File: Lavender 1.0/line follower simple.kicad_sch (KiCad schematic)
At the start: 33 parts, among them J1 XT30UPB-M, J2 Conn_01x20_MountingPin, J3 Conn_01x02_Pin, J4 Conn_01x02_Pin, J6 Conn_01x20_MountingPin, J7 Conn_01x20_MountingPin, J9 Conn_01x20_MountingPin, SW2 SW_Push, SW3 SW_Push, SW5 SW_Push_DPDT, SW6 SW_Push_DPDT, U1 74HC4067

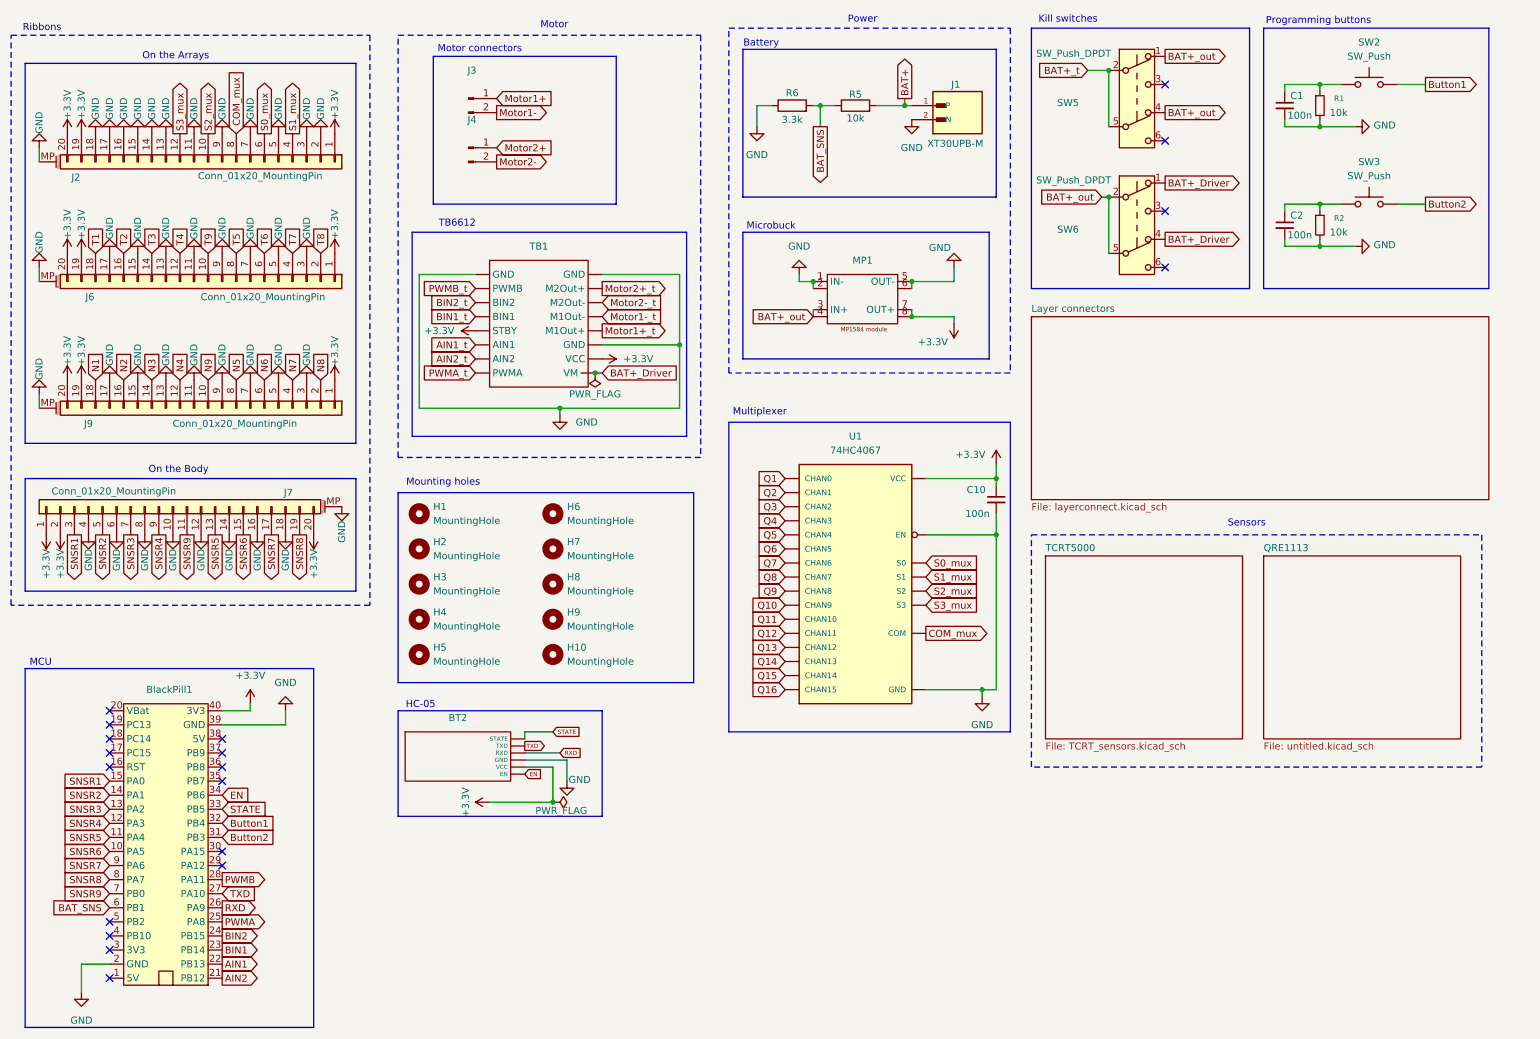
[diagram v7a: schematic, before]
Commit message: Start custom sensor array
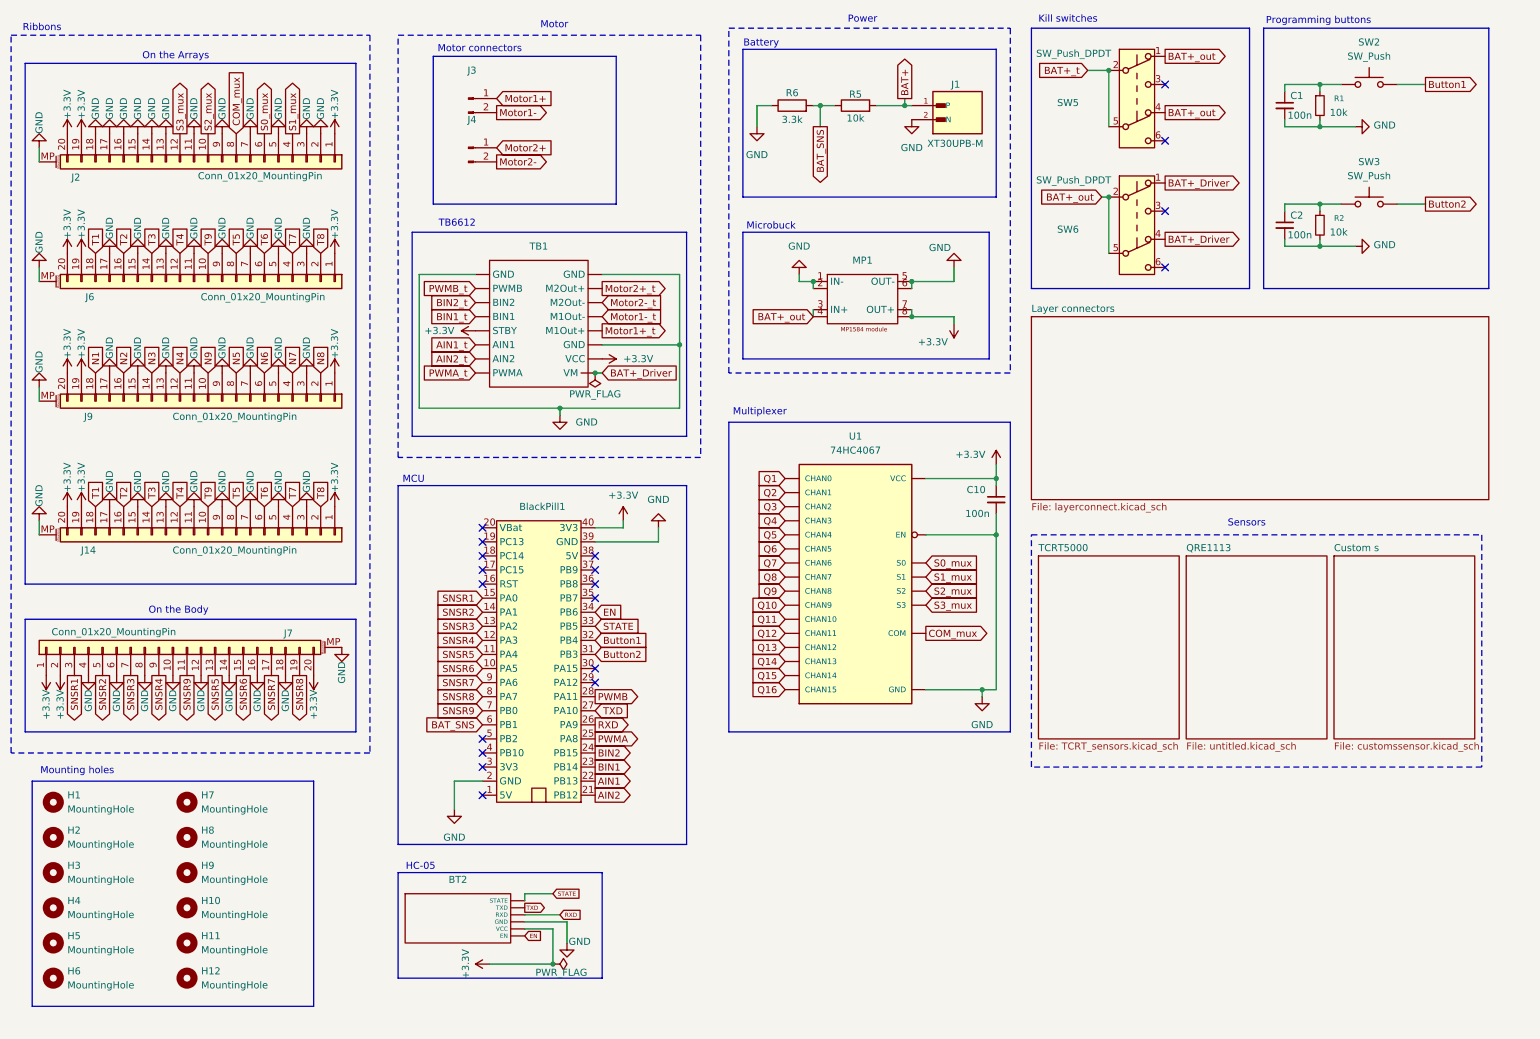
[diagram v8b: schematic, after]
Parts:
- added H11, H12: MountingHole, customs:2mm hole, symbol Mechanical:MountingHole
- added J14: Conn_01x20_MountingPin, Connector_FFC-FPC:Amphenol_F32Q-1A7x1-11020_1x20-1MP_P0.5mm_Horizontal, symbol Connector_Generic_MountingPin:Conn_01x20_MountingPin
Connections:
- net +3.3V: now also J14.1 (Pin_1), J14.19 (Pin_19), J14.20 (Pin_20)
- net GND: now also J14.11 (Pin_11), J14.13 (Pin_13), J14.15 (Pin_15), J14.17 (Pin_17), J14.3 (Pin_3), J14.5 (Pin_5), J14.7 (Pin_7), J14.9 (Pin_9), J14.MP (MountPin)
- net T1: now also J14.18 (Pin_18)
- net T2: now also J14.16 (Pin_16)
- net T3: now also J14.14 (Pin_14)
- net T4: now also J14.12 (Pin_12)
- net T5: now also J14.8 (Pin_8)
- net T6: now also J14.6 (Pin_6)
- net T7: now also J14.4 (Pin_4)
- net T8: now also J14.2 (Pin_2)
- net T9: now also J14.10 (Pin_10)
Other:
- added sheet Custom s (customssensor.kicad_sch)
- moved on the sheet: BT2, BlackPill1, H1, H10, H2, H3, H4, H5, H6, H7, H8, H9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
